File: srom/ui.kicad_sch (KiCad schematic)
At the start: 6 parts, among them J301 Conn_01x05_Female, J302 Conn_01x04_Female, J303 Conn_01x03_Female, J304 Conn_01x06_Female, U301 Pico-3 UI

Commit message: add some LEDs to schematic
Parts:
- added D301: LED_Small, LED_THT:LED_D3.0mm, symbol Device:LED_Small
- added R301: R330, Resistor_SMD:R_1206_3216Metric_Pad1.30x1.75mm_HandSolder, symbol Device:R
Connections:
- net GND: now also D301.1 (K)
- net INSERTED: now reaches U301.15 (GPIO11)
- net INSERTED: now also R301.1
- net MOTOR_ON: now reaches U301.32 (GPIO27_ADC1)
- new net: D301.2 (A), R301.2
- no-connect marks 22 -> 20
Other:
- note added: "For GUI, LED is direct from IO output"
- note added: "LED for inserted. Assume smallish green one, need to confirm resistor value and foot print for a suitable green LED."
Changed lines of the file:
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@@
   (no_connect (at 207.01 49.53))
   (no_connect (at 54.61 73.66))
-  (no_connect (at 54.61 71.12))
+  (no_connect (at 54.61 63.5))
   (no_connect (at 252.984 84.836))
   (no_connect (at 252.984 87.376))
-  (no_connect (at 54.61 63.5))
-  (no_connect (at 90.17 55.88))
   (no_connect (at 54.61 81.28))
   (no_connect (at 90.17 48.26))
@@
     (stroke (width 0) (type default) (color 0 0 0 0))
   )
+  (polyline (pts (xy 137.922 158.75) (xy 71.12 158.75))
+    (stroke (width 0) (type default) (color 0 0 0 0))
+  )
   (polyline (pts (xy 132.08 21.59) (xy 132.08 78.74))
     (stroke (width 0) (type default) (color 0 0 0 0))
@@
     (stroke (width 0) (type default) (color 0 0 0 0))
   )
+  (wire (pts (xy 117.094 145.288) (xy 117.094 142.24))
+    (stroke (width 0) (type default) (color 0 0 0 0))
+  )
   (wire (pts (xy 189.23 29.21) (xy 189.23 33.655))
     (stroke (width 0) (type default) (color 0 0 0 0))
@@
     (stroke (width 0) (type default) (color 0 0 0 0))
   )
+  (polyline (pts (xy 72.39 134.62) (xy 72.39 134.874))
+    (stroke (width 0) (type default) (color 0 0 0 0))
+  )
   (polyline (pts (xy 280.67 132.08) (xy 194.31 132.08))
     (stroke (width 0) (type default) (color 0 0 0 0))
   )
+  (wire (pts (xy 107.696 142.24) (xy 112.014 142.24))
+    (stroke (width 0) (type default) (color 0 0 0 0))
+  )
   (wire (pts (xy 99.06 38.1) (xy 107.95 38.1))
     (stroke (width 0) (type default) (color 0 0 0 0))
@@
     (stroke (width 0) (type default) (color 0 0 0 0))
   )
+  (polyline (pts (xy 137.922 134.874) (xy 137.922 158.75))
+    (stroke (width 0) (type default) (color 0 0 0 0))
+  )
   (wire (pts (xy 148.59 115.57) (xy 165.1 115.57))
     (stroke (width 0) (type default) (color 0 0 0 0))
@@
     (stroke (width 0) (type default) (color 0 0 0 0))
   )
+  (polyline (pts (xy 71.12 158.75) (xy 71.12 134.62))
+    (stroke (width 0) (type default) (color 0 0 0 0))
+  )
   (wire (pts (xy 210.82 111.76) (xy 228.6 111.76))
     (stroke (width 0) (type default) (color 0 0 0 0))
@@
     (stroke (width 0) (type default) (color 0 0 0 0))
   )
+  (polyline (pts (xy 71.374 134.874) (xy 137.922 134.874))
+    (stroke (width 0) (type default) (color 0 0 0 0))
+  )
   (wire (pts (xy 30.48 40.64) (xy 30.48 53.34))
     (stroke (width 0) (type default) (color 0 0 0 0))
   )
+  (wire (pts (xy 96.774 142.24) (xy 100.076 142.24))
+    (stroke (width 0) (type default) (color 0 0 0 0))
+  )
   (wire (pts (xy 202.565 53.34) (xy 207.01 53.34))
     (stroke (width 0) (type default) (color 0 0 0 0))
@@
   (wire (pts (xy 228.6 106.68) (xy 236.22 106.68))
     (stroke (width 0) (type default) (color 0 0 0 0))
+  )
+  (text "For GUI, LED is direct\nfrom IO output" (at 103.632 57.658 0)
+    (effects (font (size 1.27 1.27)) (justify left bottom))
   )
   (text "Pico for doing user interface. Buttons, OLED screen, SD card. Talks to IO pico via UART."
@@
     (effects (font (size 1.27 1.27)) (justify left bottom))
   )
+  (text "LED for inserted. Assume smallish green one, need to confirm\nresistor value and foot print for a suitable green LED."
+    (at 74.422 156.972 0)
+    (effects (font (size 1.27 1.27)) (justify left bottom))
+  )
   (global_label "SWDCLK_P3" (shape input) (at 69.85 88.9 270) (fields_autoplaced)
     (effects (font (size 1.27 1.27)) (justify right))
@@
     )
   )
+  (global_label "MOTOR_ON" (shape input) (at 90.17 55.88 0) (fields_autoplaced)
+    (effects (font (size 1.27 1.27)) (justify left))
+    (property "Intersheet References" "${INTERSHEET_REFS}" (id 0) (at 102.5617 55.8006 0)
+      (effects (font (size 1.27 1.27)) (justify left) hide)
+    )
+  )
   (global_label "SD_CARD_DETECT" (shape output) (at 207.01 60.96 0) (fields_autoplaced)
     (effects (font (size 1.27 1.27)) (justify left))
@@
     )
   )
+  (global_label "INSERTED" (shape input) (at 96.774 142.24 180) (fields_autoplaced)
+    (effects (font (size 1.27 1.27)) (justify right))
+    (property "Intersheet References" "${INTERSHEET_REFS}" (id 0) (at 85.4104 142.1606 0)
+      (effects (font (size 1.27 1.27)) (justify right) hide)
+    )
+  )
   (global_label "3V3_PICO3" (shape input) (at 165.1 115.57 0) (fields_autoplaced)
     (effects (font (size 1.27 1.27)) (justify left))
@@
     (property "Intersheet References" "${INTERSHEET_REFS}" (id 0) (at 57.1743 152.9556 0)
       (effects (font (size 1.27 1.27)) (justify left) hide)
+    )
+  )
+  (global_label "INSERTED" (shape output) (at 54.61 71.12 180) (fields_autoplaced)
+    (effects (font (size 1.27 1.27)) (justify right))
+    (property "Intersheet References" "${INTERSHEET_REFS}" (id 0) (at 43.2464 71.0406 0)
+      (effects (font (size 1.27 1.27)) (justify right) hide)
     )
   )
@@
     )
     (property "Datasheet" "~" (id 3) (at 99.06 38.1 0)
+      (effects (font (size 1.27 1.27)) hide)
+    )
+    (pin "1")
+  )
+  (symbol (lib_id "power:GND") (at 117.094 145.288 0) (unit 1)
+    (in_bom yes) (on_board yes) (fields_autoplaced)
+    (property "Reference" "#PWR0107" (id 0) (at 117.094 151.638 0)
+      (effects (font (size 1.27 1.27)) hide)
+    )
+    (property "Value" "GND" (id 1) (at 117.094 150.622 0))
+    (property "Footprint" "" (id 2) (at 117.094 145.288 0)
+      (effects (font (size 1.27 1.27)) hide)
+    )
+    (property "Datasheet" "" (id 3) (at 117.094 145.288 0)
       (effects (font (size 1.27 1.27)) hide)
     )
@@
     (pin "8")
     (pin "9")
+  )
+  (symbol (lib_id "Device:R") (at 103.886 142.24 90) (unit 1)
+    (in_bom yes) (on_board yes) (fields_autoplaced)
+    (property "Reference" "R301" (id 0) (at 103.886 136.144 90))
+    (property "Value" "R330" (id 1) (at 103.886 138.684 90))
+    (property "Footprint" "Resistor_SMD:R_1206_3216Metric_Pad1.30x1.75mm_HandSolder" (id 2) (at 103.886 144.018 90)
+      (effects (font (size 1.27 1.27)) hide)
+    )
+    (property "Datasheet" "~" (id 3) (at 103.886 142.24 0)
+      (effects (font (size 1.27 1.27)) hide)
+    )
+    (pin "1")
+    (pin "2")
   )
   (symbol (lib_id "power:GND") (at 171.45 107.95 0) (unit 1)
@@
     (pin "5")
   )
+  (symbol (lib_id "Device:LED_Small") (at 114.554 142.24 180) (unit 1)
+    (in_bom yes) (on_board yes) (fields_autoplaced)
+    (property "Reference" "D301" (id 0) (at 114.4905 136.144 0))
+    (property "Value" "LED_Small" (id 1) (at 114.4905 138.684 0))
+    (property "Footprint" "LED_THT:LED_D3.0mm" (id 2) (at 114.554 142.24 90)
+      (effects (font (size 1.27 1.27)) hide)
+    )
+    (property "Datasheet" "~" (id 3) (at 114.554 142.24 90)
+      (effects (font (size 1.27 1.27)) hide)
+    )
+    (pin "1")
+    (pin "2")
+  )
   (symbol (lib_id "power:GND") (at 236.22 106.68 0) (unit 1)

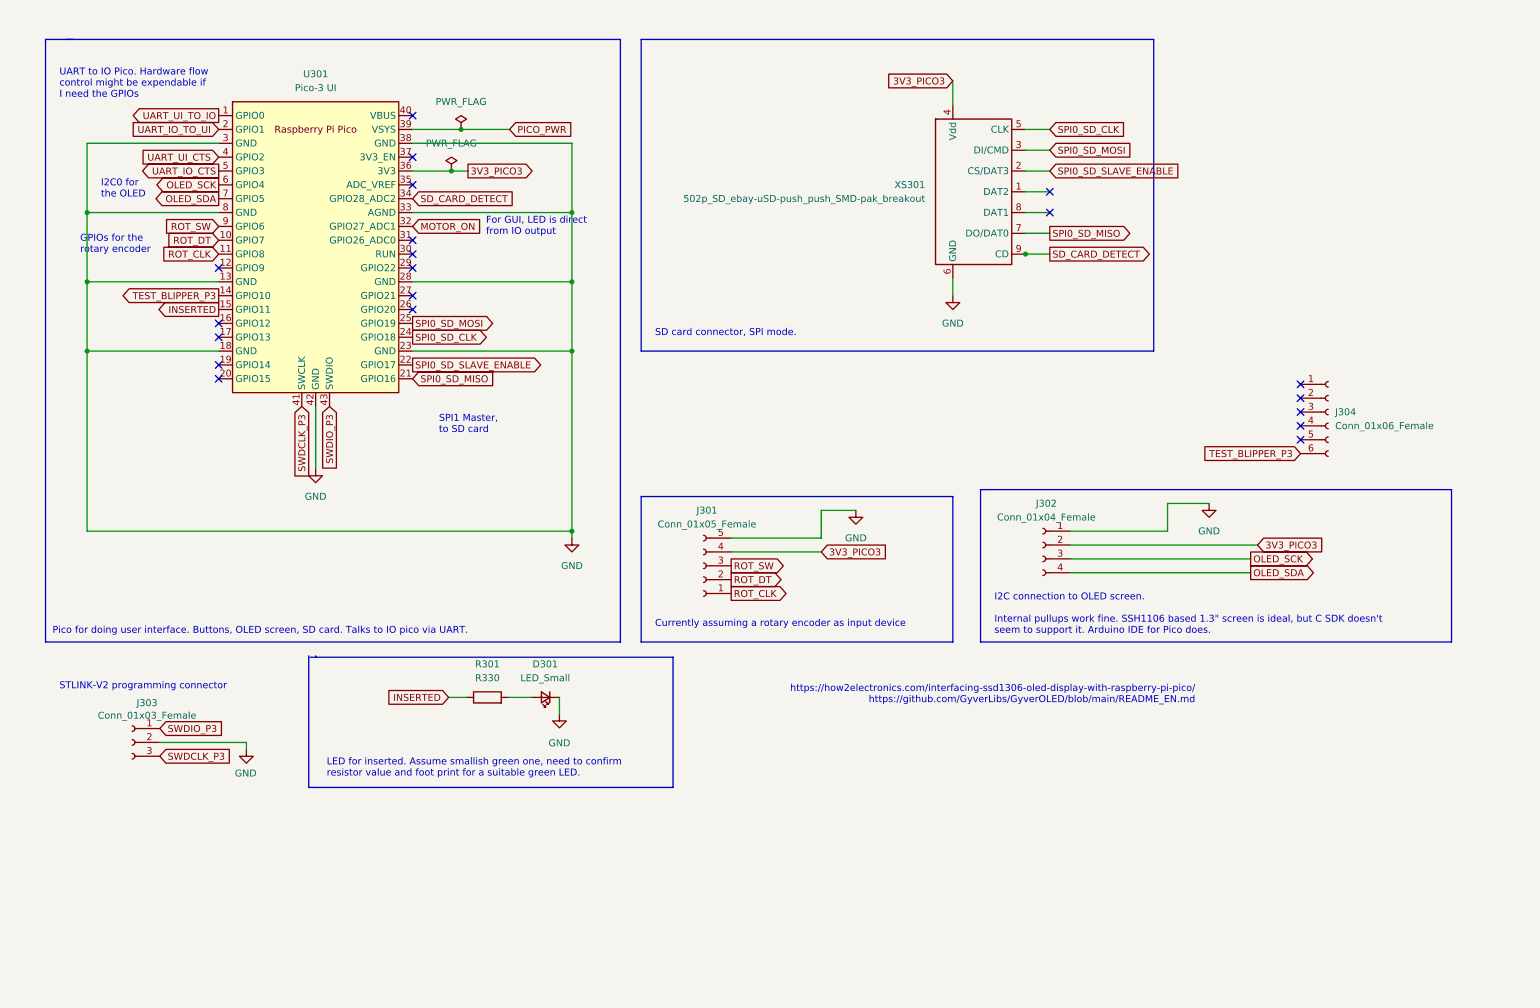
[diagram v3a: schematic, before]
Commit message: add 2 switches as buttons for the UI
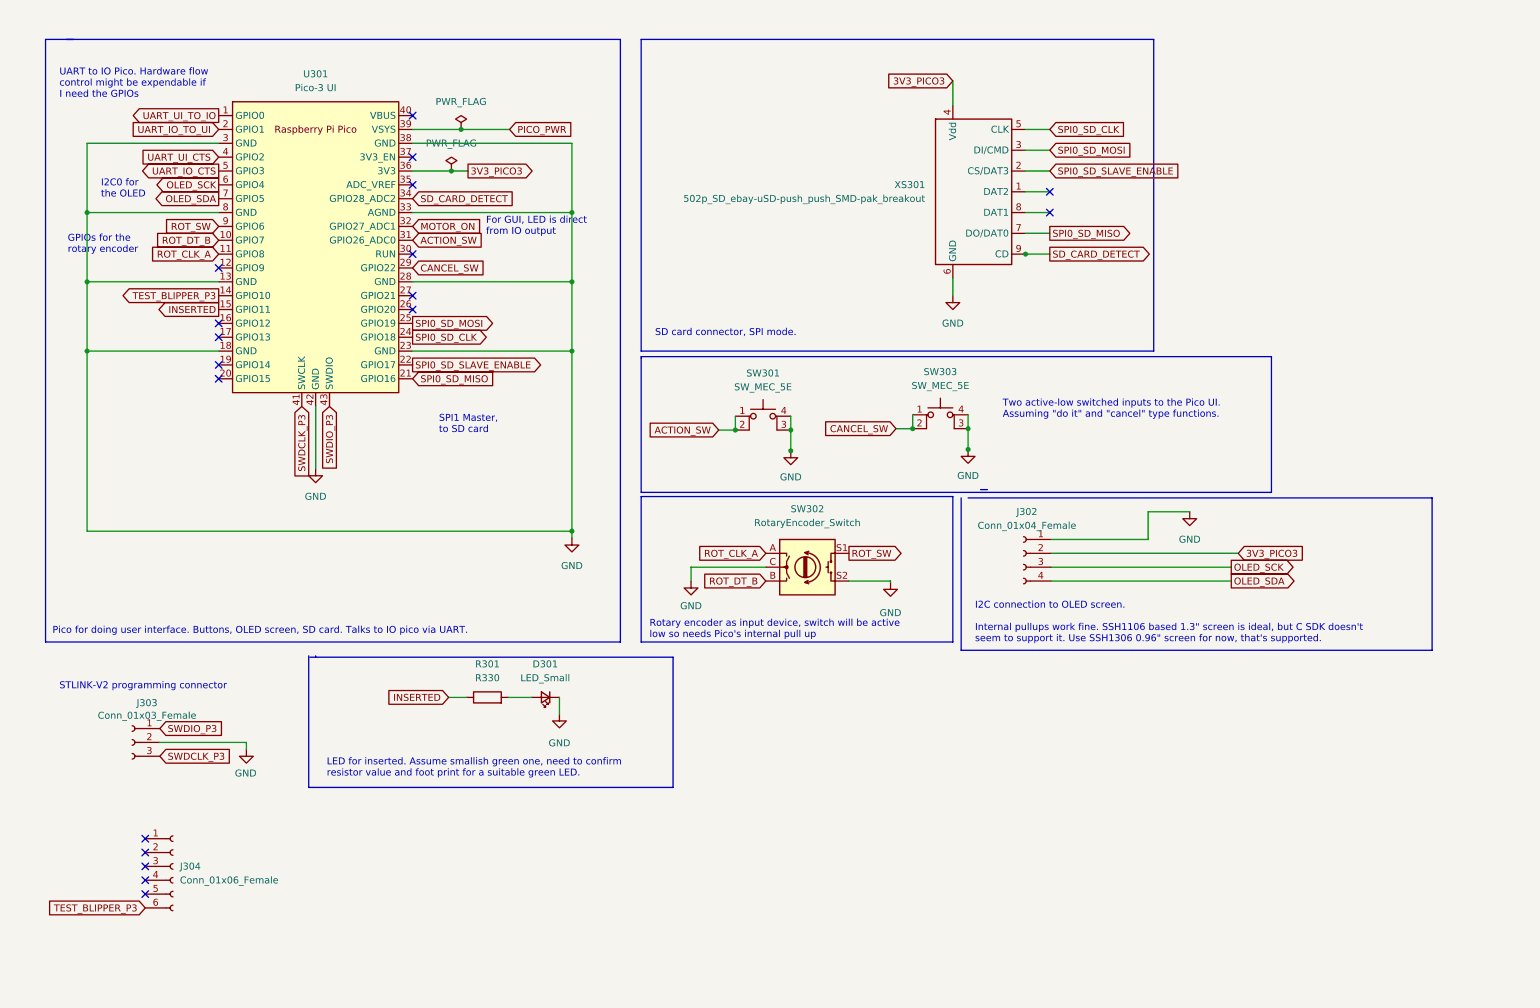
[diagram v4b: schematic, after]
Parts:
- removed J301: Conn_01x05_Female, Connector_PinHeader_2.54mm:PinHeader_1x05_P2.54mm_Vertical, symbol Connector:Conn_01x05_Female
- added SW301, SW303: SW_MEC_5E, Button_Switch_THT:SW_PUSH_6mm_H4.3mm, symbol Switch:SW_MEC_5E
- added SW302: RotaryEncoder_Switch, Rotary_Encoder:RotaryEncoder_Bourns_Vertical_PEC12R-3xxxF-Sxxxx, symbol Device:RotaryEncoder_Switch
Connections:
- net GND: now also SW301.3 (K), SW301.4 (A), SW302.C, SW302.S2, SW303.3 (K), SW303.4 (A)
- net ROT_SW: now also SW302.S1
- net CANCEL_SW: now reaches U301.29 (GPIO22)
- net CANCEL_SW: now also SW303.1, SW303.2
- net ACTION_SW: now reaches U301.31 (GPIO26_ADC0)
- net ACTION_SW: now also SW301.1, SW301.2
- net ROT_CLK renamed ROT_CLK_A
- net ROT_CLK_A: now also SW302.A
- net ROT_DT renamed ROT_DT_B
- net ROT_DT_B: now also SW302.B
- no-connect marks 20 -> 18
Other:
- note added: "I2C connection to OLED screen. Internal pullups work fine. SSH1106 based 1.3" screen is ideal, but C SDK doesn't seem to support it. Use SSH1306 0.96" screen for now, that's supported."
- note added: "Rotary encoder as input device, switch will be active low so needs Pico's internal pull up"
- note added: "Two active-low switched inputs to the Pico UI. Assuming "do it" and "cancel" type functions."
- note removed: "Currently assuming a rotary encoder as input device"
- note removed: "I2C connection to OLED screen. Internal pullups work fine. SSH1106 based 1.3" screen is ideal, but C SDK doesn't seem to support it. Arduino IDE for Pico does."
- note removed: "https://how2electronics.com/interfacing-ssd1306-oled-display-with-raspberry-pi-pico/ https://github.com/GyverLibs/GyverOLED/blob/main/README_EN.md"
- moved on the sheet: J302, J304

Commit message: update schematic, remove uart UI/IO link, replace with PIO link
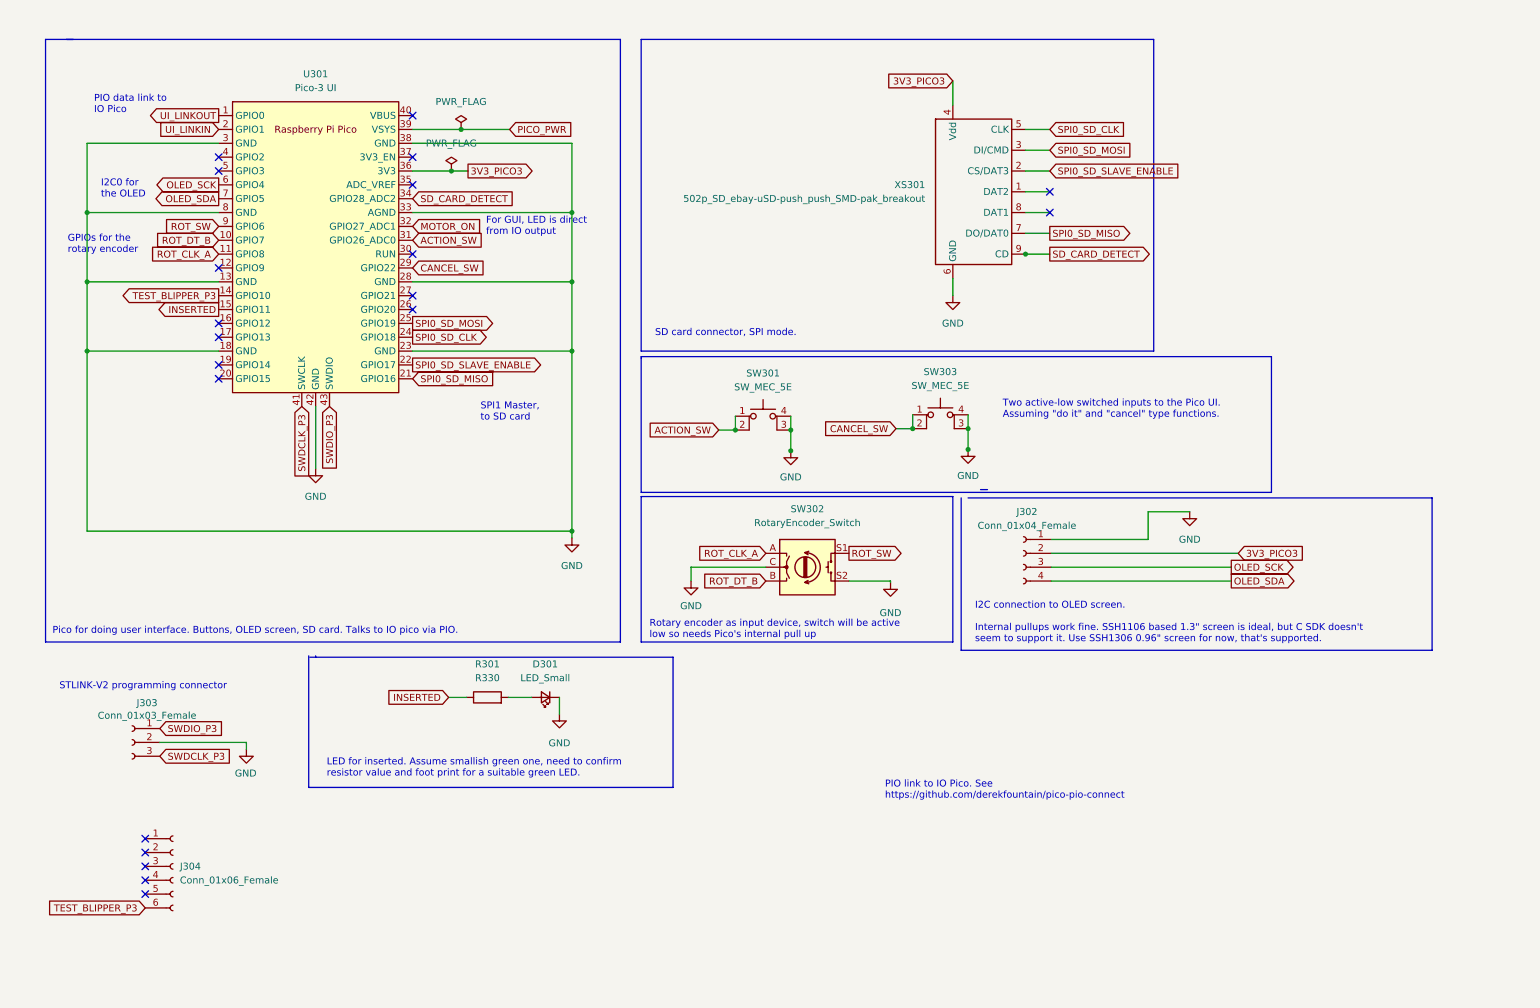
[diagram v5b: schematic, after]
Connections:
- net UART_IO_CTS: no longer names the net of U301.5 (GPIO3)
- net UART_IO_TO_UI renamed UI_LINKIN
- net UART_UI_CTS: no longer names the net of U301.4 (GPIO2)
- net UART_UI_TO_IO renamed UI_LINKOUT
- no-connect marks 18 -> 20
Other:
- note added: "PIO data link to IO Pico"
- note added: "PIO link to IO Pico. See https://github.com/derekfountain/pico-pio-connect"
- note added: "Pico for doing user interface. Buttons, OLED screen, SD card. Talks to IO pico via PIO."
- note removed: "Pico for doing user interface. Buttons, OLED screen, SD card. Talks to IO pico via UART."
- note removed: "UART to IO Pico. Hardware flow control might be expendable if I need the GPIOs"
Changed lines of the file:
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@@
   (no_connect (at 90.17 68.58))
   (no_connect (at 90.17 60.96))
+  (no_connect (at 54.61 43.18))
   (no_connect (at 90.17 71.12))
   (no_connect (at 54.61 83.82))
+  (no_connect (at 54.61 45.72))
   (no_connect (at 207.01 53.34))
   (no_connect (at 41.148 173.228))
@@
     (effects (font (size 1.27 1.27)) (justify left bottom))
   )
-  (text "Pico for doing user interface. Buttons, OLED screen, SD card. Talks to IO pico via UART."
+  (text "Pico for doing user interface. Buttons, OLED screen, SD card. Talks to IO pico via PIO."
     (at 24.13 130.81 0)
+    (effects (font (size 1.27 1.27)) (justify left bottom))
+  )
+  (text "PIO data link to\nIO Pico" (at 31.75 35.306 0)
     (effects (font (size 1.27 1.27)) (justify left bottom))
   )
@@
     (effects (font (size 1.27 1.27)) (justify left bottom))
   )
-  (text "UART to IO Pico. Hardware flow\ncontrol might be expendable if\nI need the GPIOs"
-    (at 25.4 32.512 0)
-    (effects (font (size 1.27 1.27)) (justify left bottom))
-  )
-  (text "SPI1 Master,\nto SD card" (at 94.996 93.98 0)
+  (text "PIO link to IO Pico. See\nhttps://github.com/derekfountain/pico-pio-connect"
+    (at 176.784 161.036 0)
+    (effects (font (size 1.27 1.27)) (justify left bottom))
+  )
+  (text "SPI1 Master,\nto SD card" (at 102.616 91.694 0)
     (effects (font (size 1.27 1.27)) (justify left bottom))
   )
@@
     )
   )
-  (global_label "UART_UI_CTS" (shape input) (at 54.61 43.18 180) (fields_autoplaced)
-    (effects (font (size 1.27 1.27)) (justify right))
-    (property "Intersheet References" "${INTERSHEET_REFS}" (id 0) (at 40.2226 43.1006 0)
-      (effects (font (size 1.27 1.27)) (justify right) hide)
-    )
-  )
   (global_label "3V3_PICO3" (shape output) (at 100.33 45.72 0) (fields_autoplaced)
     (effects (font (size 1.27 1.27)) (justify left))
@@
     )
   )
-  (global_label "UART_UI_TO_IO" (shape output) (at 54.61 35.56 180) (fields_autoplaced)
-    (effects (font (size 1.27 1.27)) (justify right))
-    (property "Intersheet References" "${INTERSHEET_REFS}" (id 0) (at 38.4688 35.4806 0)
-      (effects (font (size 1.27 1.27)) (justify right) hide)
-    )
-  )
-  (global_label "UART_IO_CTS" (shape output) (at 54.61 45.72 180) (fields_autoplaced)
-    (effects (font (size 1.27 1.27)) (justify right))
-    (property "Intersheet References" "${INTERSHEET_REFS}" (id 0) (at 40.2226 45.6406 0)
+  (global_label "UI_LINKOUT" (shape output) (at 54.61 35.56 180) (fields_autoplaced)
+    (effects (font (size 1.27 1.27)) (justify right))
+    (property "Intersheet References" "${INTERSHEET_REFS}" (id 0) (at 41.4321 35.4806 0)
       (effects (font (size 1.27 1.27)) (justify right) hide)
     )
@@
     )
   )
-  (global_label "UART_IO_TO_UI" (shape input) (at 54.61 38.1 180) (fields_autoplaced)
-    (effects (font (size 1.27 1.27)) (justify right))
-    (property "Intersheet References" "${INTERSHEET_REFS}" (id 0) (at 38.4688 38.0206 0)
-      (effects (font (size 1.27 1.27)) (justify right) hide)
-    )
+  (global_label "UI_LINKIN" (shape input) (at 54.61 38.1 180) (fields_autoplaced)
+    (effects (font (size 1.27 1.27)) (justify right))
+    (property "Intersheet References" "${INTERSHEET_REFS}" (id 0) (at 43.1255 38.0206 0)
+      (effects (font (size 1.27 1.27)) (justify right) hide)
+    )
